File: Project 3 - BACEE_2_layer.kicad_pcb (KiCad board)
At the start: 2 copper layers, 40.4 x 29.7 mm, 17 parts, among them J1 Digital pins, J2 Serial, J3 ICSP, J4 I2C, U1 DS1337S, U2 24LC1025, U3 24LC1025, U4 ATMEGA328P-AU, Y1 Crystal 32 MHz, Y2 Crystal 16 MHz

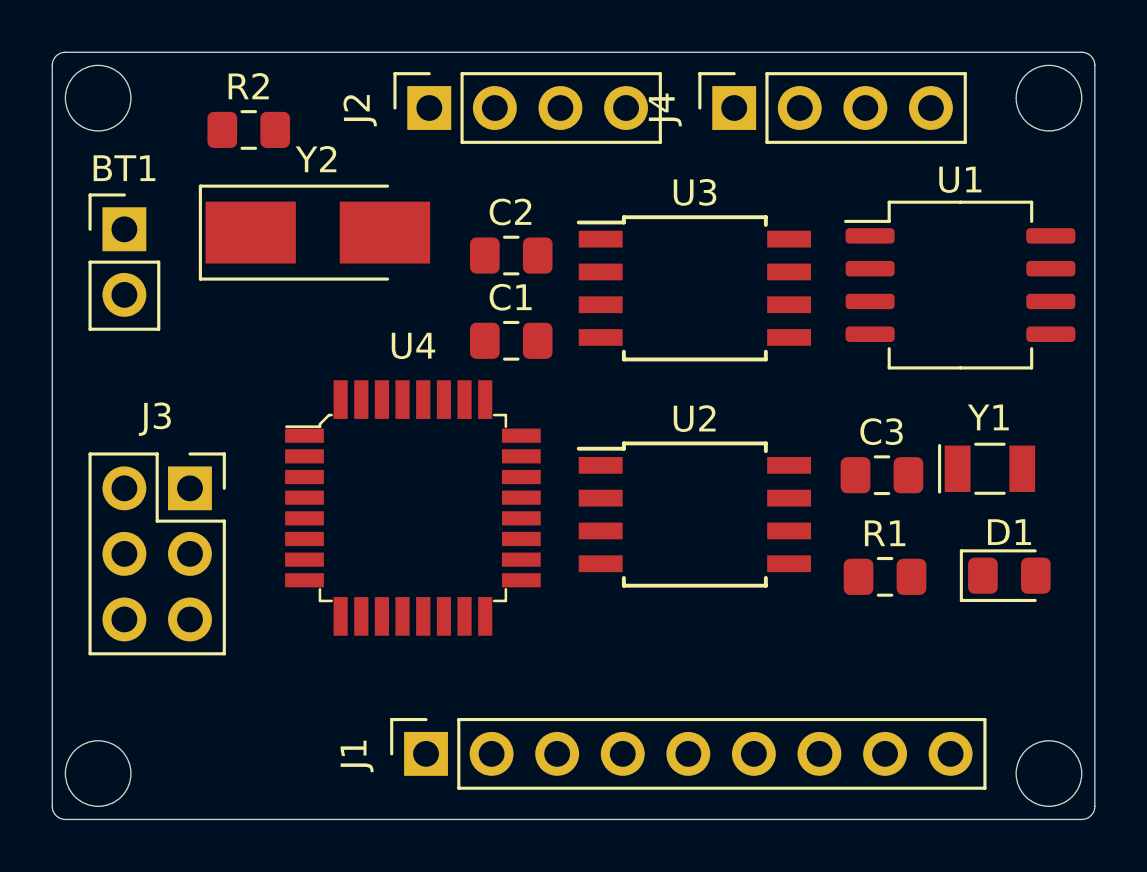
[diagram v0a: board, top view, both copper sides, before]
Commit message: Fully routed board in two layers.
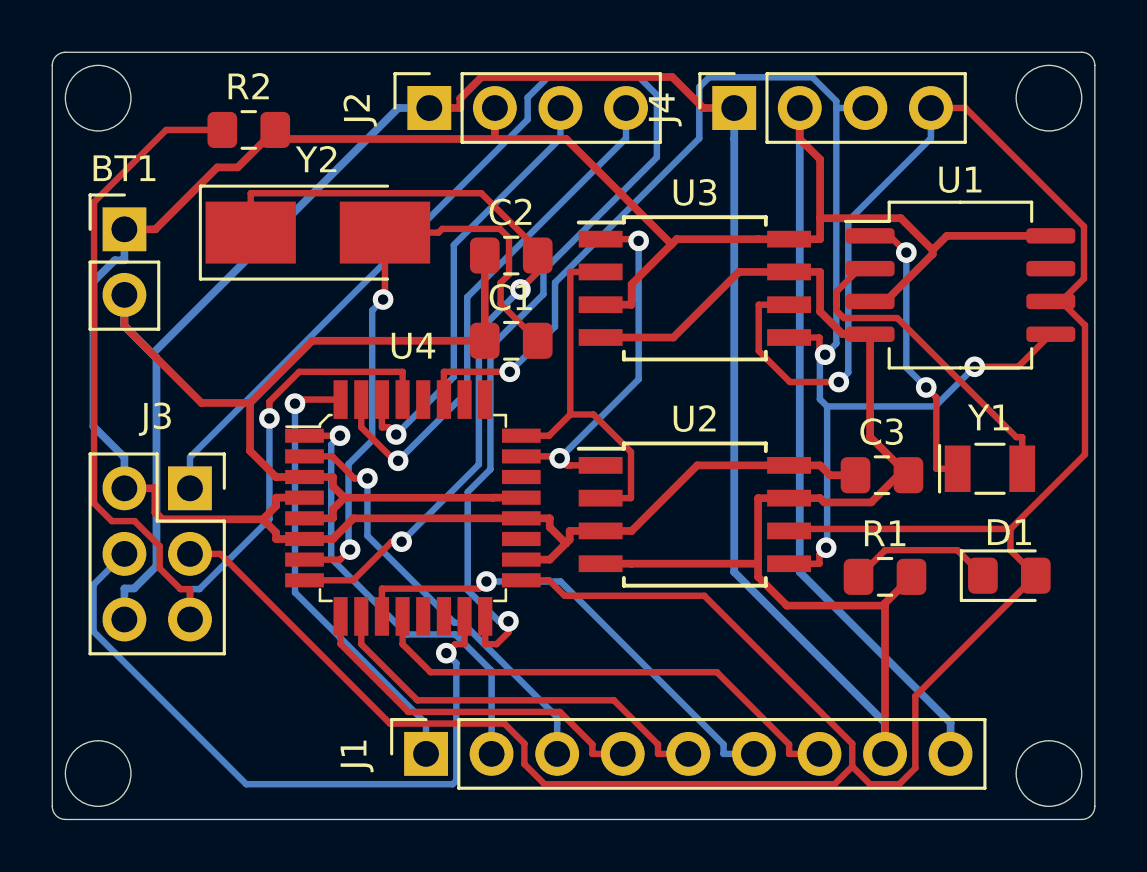
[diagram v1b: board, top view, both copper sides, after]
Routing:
- net GNDPWR: track 0.00 -> 152.6 mm
- net /VCC: track 0.00 -> 129.5 mm
- net /SCK: track 0.00 -> 110.2 mm, vias 0 -> 1
- net /SDA: track 0.00 -> 56.0 mm, vias 0 -> 4
- net /MISO: track 0.00 -> 53.1 mm, vias 0 -> 1
- net /RESET: track 0.00 -> 41.2 mm, vias 0 -> 1
- net Net-(C2-Pad2): track 0.00 -> 31.4 mm, vias 0 -> 2
- net /MOSI: track 0.00 -> 27.1 mm, vias 0 -> 1
- net Net-(C1-Pad2): track 0.00 -> 24.5 mm, vias 0 -> 2
- net /TX: track 0.00 -> 20.4 mm, vias 0 -> 1
- net /D8: track 0.00 -> 19.2 mm
- net /D7: track 0.00 -> 18.6 mm, vias 0 -> 1
- net /D2: track 0.00 -> 17.5 mm, vias 0 -> 1
- net /D3: track 0.00 -> 17.5 mm, vias 0 -> 1
- net /RX: track 0.00 -> 17.0 mm, vias 0 -> 1
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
